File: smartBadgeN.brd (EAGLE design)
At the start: 82 x 68 mm, 62 parts, among them IC1 SI1304BDL, J1 10118192-0001LF, J2 LiPo, J3 505278-2433, Q1 MBT3904DW1T1, Q2 2.5A/30V, U1 CP2102N, U2 AP2112K-3.3V, U3 ESP-WROOM-32, U4 MCP73831

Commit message: revB init
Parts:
- C3: value 0.1uF -> 10uF
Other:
- outline, holes or cut-outs redrawn
- board text added: "SmartBadge rev B"
- board text removed: "SmartBadge rev A"
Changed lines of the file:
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@@
 <setting verticaltext="up"/>
 </settings>
-<grid distance="0.02" unitdist="mm" unit="mm" style="lines" multiple="1" display="yes" altdistance="0.5" altunitdist="mm" altunit="mm"/>
+<grid distance="0.1" unitdist="mm" unit="mm" style="lines" multiple="1" display="yes" altdistance="0.5" altunitdist="mm" altunit="mm"/>
 <layers>
 <layer number="1" name="Top" color="4" fill="1" visible="yes" active="yes"/>
@@
 <wire x1="3" y1="0" x2="79" y2="0" width="0" layer="20"/>
 <wire x1="82" y1="3" x2="82" y2="59" width="0" layer="20"/>
-<wire x1="79" y1="62" x2="57" y2="62" width="0" layer="20"/>
-<wire x1="26" y1="62" x2="3" y2="62" width="0" layer="20"/>
+<wire x1="79" y1="62" x2="55" y2="62" width="0" layer="20"/>
+<wire x1="27" y1="62" x2="3" y2="62" width="0" layer="20"/>
 <wire x1="0" y1="59" x2="0" y2="3" width="0" layer="20"/>
-<wire x1="49.5" y1="62" x2="33.5" y2="62" width="0" layer="20"/>
-<wire x1="49.5" y1="66" x2="33.5" y2="66" width="0" layer="20"/>
-<wire x1="33.5" y1="66" x2="33.5" y2="62" width="0" layer="20" curve="180"/>
-<wire x1="49.5" y1="66" x2="49.5" y2="62" width="0" layer="20" curve="-180"/>
+<wire x1="46.68" y1="61" x2="35.3" y2="61" width="0" layer="20"/>
+<wire x1="46.68" y1="64.5" x2="43.4" y2="64.5" width="0" layer="20"/>
+<wire x1="38.6" y1="64.5" x2="35.3" y2="64.5" width="0" layer="20"/>
+<wire x1="35.3" y1="64.5" x2="35.3" y2="61" width="0" layer="20" curve="180"/>
+<wire x1="46.68" y1="64.5" x2="46.68" y2="61" width="0" layer="20" curve="-180"/>
 <wire x1="4.61" y1="4.26" x2="4.61" y2="34.26" width="0.1524" layer="51"/>
 <wire x1="4.61" y1="34.26" x2="54.61" y2="34.26" width="0.1524" layer="51"/>
@@
 <wire x1="79" y1="0" x2="82" y2="3" width="0" layer="20" curve="90"/>
 <wire x1="3" y1="0" x2="0" y2="3" width="0" layer="20" curve="-90"/>
-<wire x1="26" y1="62" x2="29" y2="65" width="0" layer="20" curve="90"/>
-<wire x1="29" y1="65" x2="32" y2="68" width="0" layer="20" curve="-90"/>
-<wire x1="57" y1="62" x2="54" y2="65" width="0" layer="20" curve="-90"/>
-<wire x1="51" y1="68" x2="54" y2="65" width="0" layer="20" curve="-90"/>
-<wire x1="32" y1="68" x2="51" y2="68" width="0" layer="20"/>
+<wire x1="27" y1="62" x2="30" y2="65" width="0" layer="20" curve="90"/>
+<wire x1="30" y1="65" x2="33" y2="68" width="0" layer="20" curve="-90"/>
+<wire x1="55" y1="62" x2="52" y2="65" width="0" layer="20" curve="-90"/>
+<wire x1="49" y1="68" x2="52" y2="65" width="0" layer="20" curve="-90"/>
+<wire x1="33" y1="68" x2="49" y2="68" width="0" layer="20"/>
 <text x="55.23" y="46.92" size="0.8128" layer="25" align="bottom-center">CHG</text>
 <wire x1="1.5" y1="20" x2="80.5" y2="20" width="0.1524" layer="52"/>
@@
 <wire x1="1.5" y1="56.75" x2="1.5" y2="20" width="0.1524" layer="52"/>
 <text x="12.29" y="37.13" size="0.8128" layer="25" rot="R180" align="bottom-center">RESET</text>
-<text x="79.49" y="4.82" size="1.016" layer="25" font="vector" rot="R90">SmartBadge rev A</text>
+<text x="79.49" y="4.82" size="1.016" layer="25" font="vector" rot="R90">SmartBadge rev B</text>
 <text x="4.97" y="2.48" size="0.8128" layer="25" font="vector">iotfablab.eu c/o BIBA - Bremer Institut für Produktion und Logistik GmbH</text>
 <dimension x1="0" y1="63.3" x2="82" y2="63" x3="41" y3="72.2" textsize="1.016" layer="51" dtype="horizontal" width="0.1"/>
@@
 <rectangle x1="74.83" y1="60.33" x2="75.33" y2="60.35" layer="30"/>
 <rectangle x1="74.89" y1="60.35" x2="75.23" y2="60.37" layer="30"/>
+<wire x1="38.6" y1="64.5" x2="43.4" y2="64.5" width="0" layer="20" curve="-163.40571"/>
 </plain>
 <attributes>
@@
 </autorouter>
 <elements>
-<element name="C3" library="resistor" library_urn="urn:adsk.eagle:library:348" package="C0603" package3d_urn="urn:adsk.eagle:package:23616/2" value="0.1uF" x="74.7" y="24.78" smashed="yes" rot="R270">
+<element name="C3" library="resistor" library_urn="urn:adsk.eagle:library:348" package="C0603" package3d_urn="urn:adsk.eagle:package:23616/2" value="10uF" x="74.7" y="24.78" smashed="yes" rot="R270">
 <attribute name="NAME" x="73.87" y="26.4" size="0.6096" layer="25"/>
 </element>

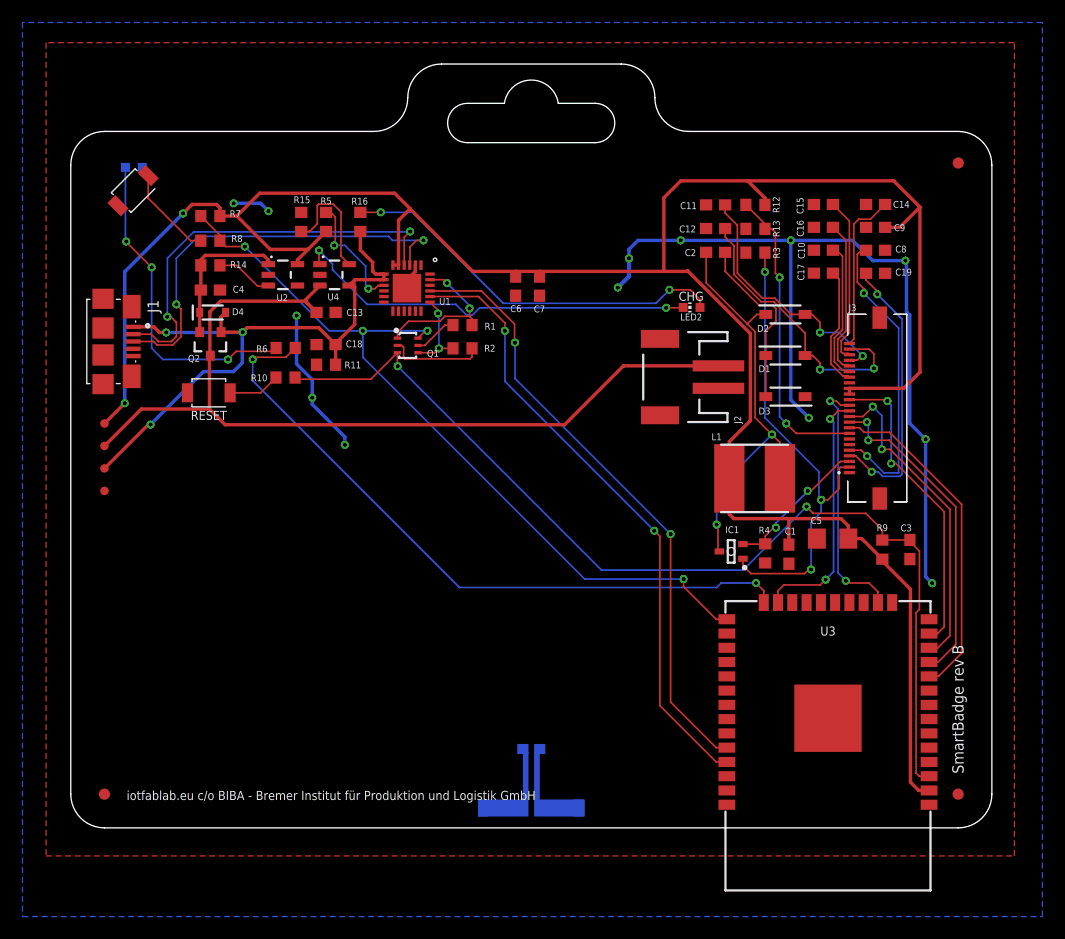
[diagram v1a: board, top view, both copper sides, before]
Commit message: capacitor values updated
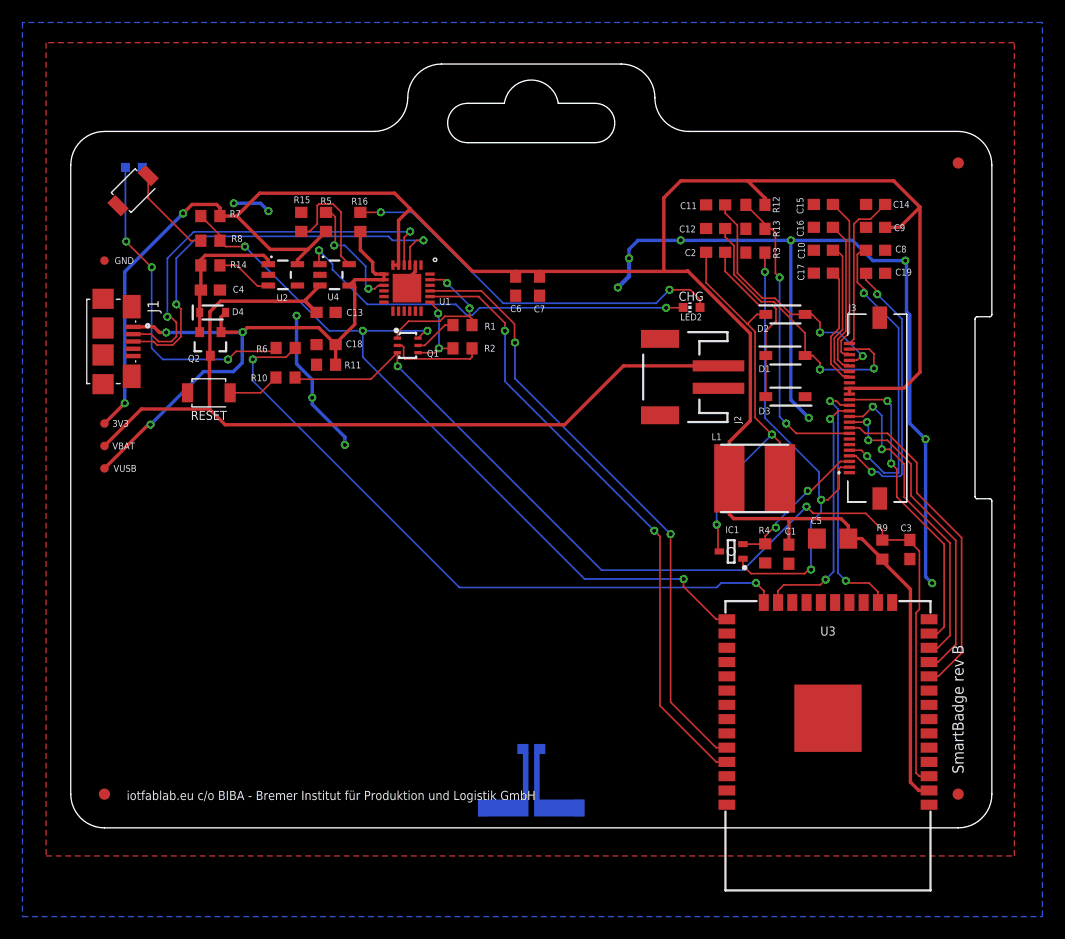
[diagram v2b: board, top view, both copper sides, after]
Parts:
- C1: value 0.1uF -> 4.7uF
- moved TP1 20.5 mm to (3.00, 50.5)
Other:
- outline, holes or cut-outs redrawn
- board text added: "3V3"
- board text added: "GND"
- board text added: "VBAT"
- board text added: "VUSB"

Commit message: schematics pdf added
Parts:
- removed J3: 505278-2433, SamacSys_Parts:5052782433
- added EPD: MOLEX-FPC-CONN-24X0.5, BIBA:MOLEX-0512812494
- turned D2 to 180 degrees
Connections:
- removed net N$15: C8.1, J3.5
- removed net N$16: C19.1, J3.4
- removed net N$24: C17.1, J3.18
- removed net N$25: C16.1, J3.20
- removed net N$26: C15.1, J3.22
- removed net N$27: C14.1, J3.24
- removed net N$33: C10.1, J3.19
- new net N$10: C16.1, EPD.P$20
- new net N$12: C15.1, EPD.P$22
- new net N$14: C14.1, EPD.P$24
- new net N$2: C17.1, EPD.P$18
- new net N$3: C10.1, EPD.P$19
- new net N$8: C19.1, EPD.P$4
- new net N$9: C8.1, EPD.P$5
- net 3V3: now also EPD.P$15, EPD.P$16; no longer J3.15, J3.16
- net BS: now also EPD.P$8; no longer J3.8
- net GDR: now also EPD.P$2; no longer J3.2
- net GND: now also EPD.P$17; no longer J3.17
- net IO13: now also EPD.P$13; no longer J3.13
- net IO14: now also EPD.P$14; no longer J3.14
- net IO15: now also EPD.P$12; no longer J3.12
- net IO25: now also EPD.P$9; no longer J3.9
- net IO26: now also EPD.P$10; no longer J3.10
- net IO27: now also EPD.P$11; no longer J3.11
- net N$18: now also D2.2; no longer D2.1
- net PREVGH: now also D2.1, EPD.P$21; no longer D2.2, J3.21
- net PREVGL: now also EPD.P$23; no longer J3.23
- net RESE: now also EPD.P$3; no longer J3.3
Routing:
- net N$14: track 0.00 -> 28.5 mm, vias 0 -> 2
- net N$12: track 0.00 -> 27.3 mm, vias 0 -> 2
- net N$15: track 27.1 -> 0.00 mm, vias 2 -> 0
- net GND: track 94.7 -> 69.9 mm, vias 13 -> 15
- net N$16: track 24.7 -> 0.00 mm, vias 2 -> 0
- net N$10: track 0.00 -> 23.3 mm, vias 0 -> 2
- net N$3: track 0.00 -> 20.5 mm, vias 0 -> 2
- net N$2: track 0.00 -> 17.3 mm, vias 0 -> 2
- net 3V3: track 215.4 -> 198.5 mm, vias 2 -> 4
- net N$26: track 14.9 -> 0.00 mm
- net N$27: track 14.3 -> 0.00 mm
- net N$9: track 0.00 -> 14.0 mm
- net N$25: track 13.8 -> 0.00 mm
- net N$33: track 12.5 -> 0.00 mm
- net N$24: track 10.8 -> 0.00 mm
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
